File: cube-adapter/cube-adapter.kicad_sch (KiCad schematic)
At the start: 40 parts, among them J1 Conn_01x02, J10 Conn_01x02, J11 Conn_01x03, J12 Conn_01x03, J13 Conn_01x03, J14 Conn_01x03, J15 Conn_01x03, J16 Conn_01x03, J17 Conn_01x03, J18 Conn_01x03, J19 Conn_01x03, J2 Conn_01x02, J20 Conn_01x03, J21 Conn_01x03, J22 Conn_01x03, J23 Conn_01x06, J24 Conn_01x06, J25 Conn_01x04, J26 Conn_01x04, J27 Conn_01x05, J28 Conn_01x05, J29 Conn_01x05, J3 Conn_01x02, J30 Conn_01x04, J31 Conn_01x04, J32 Conn_01x04, J33 Conn_01x03, J34 Conn_01x03, J35 Conn_01x03, J36 Conn_01x02, J37 Conn_01x02, J38 Conn_01x02, J4 Conn_01x02, J5 Conn_01x02, J6 Conn_01x02, J7 Conn_01x02, J8 Conn_01x02, J9 Conn_01x02, U1 MEGA_PRO_EMBED_CH340G___ATMEG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

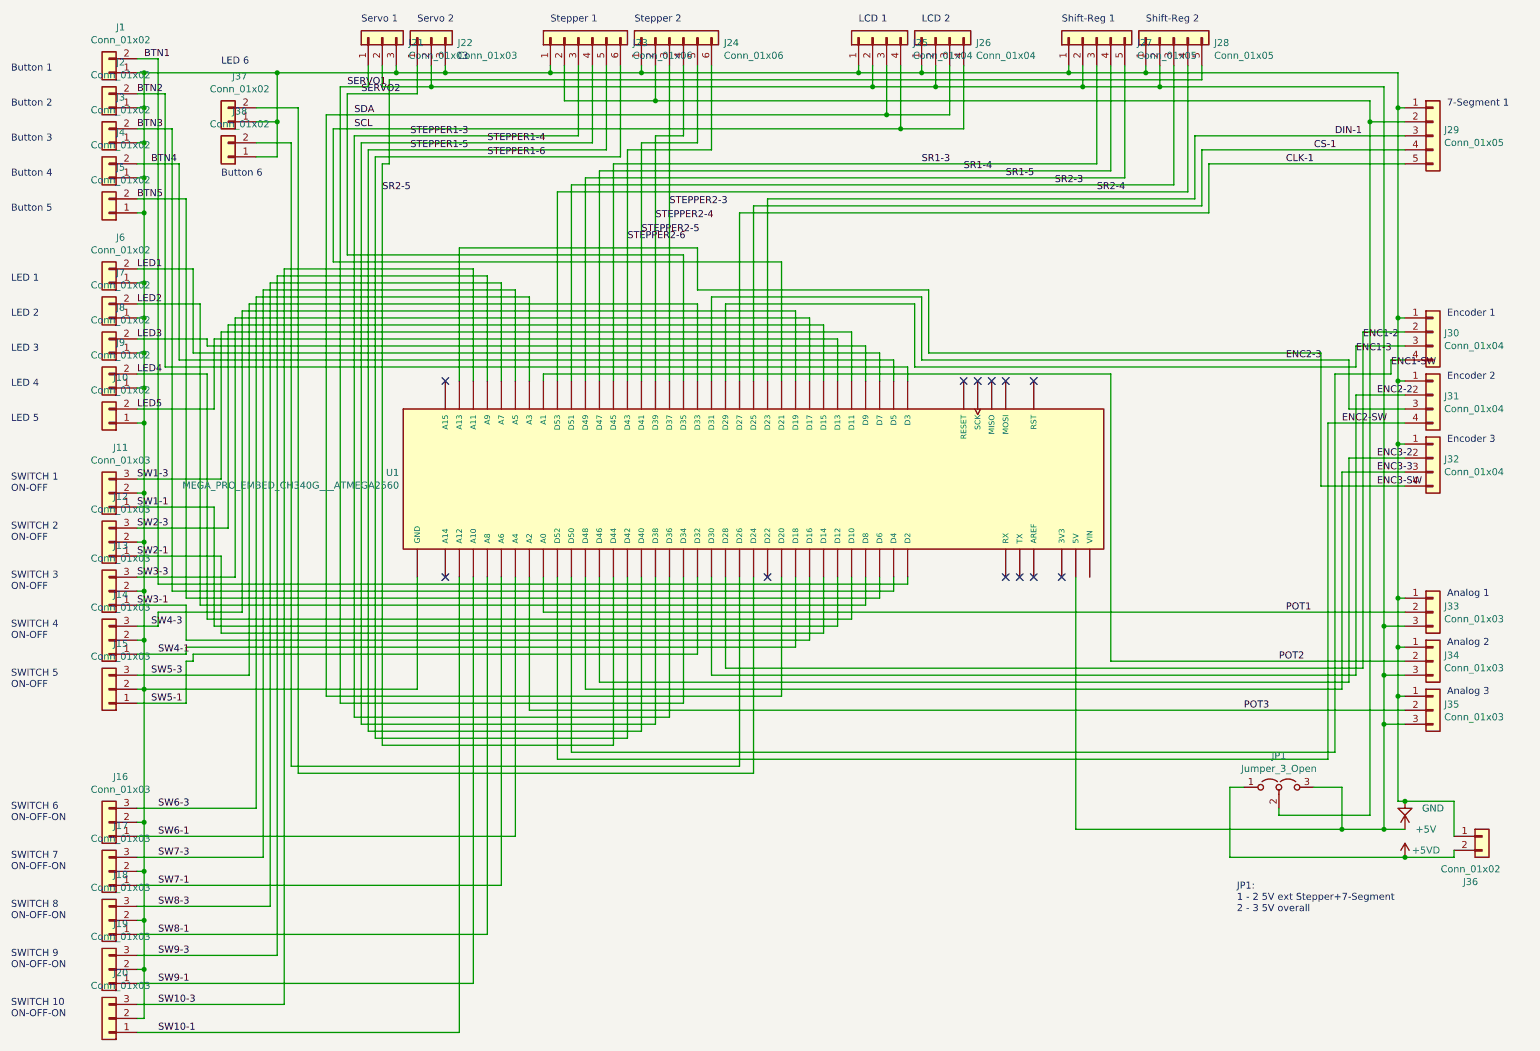
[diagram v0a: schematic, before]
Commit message: Added the cube adapter changes
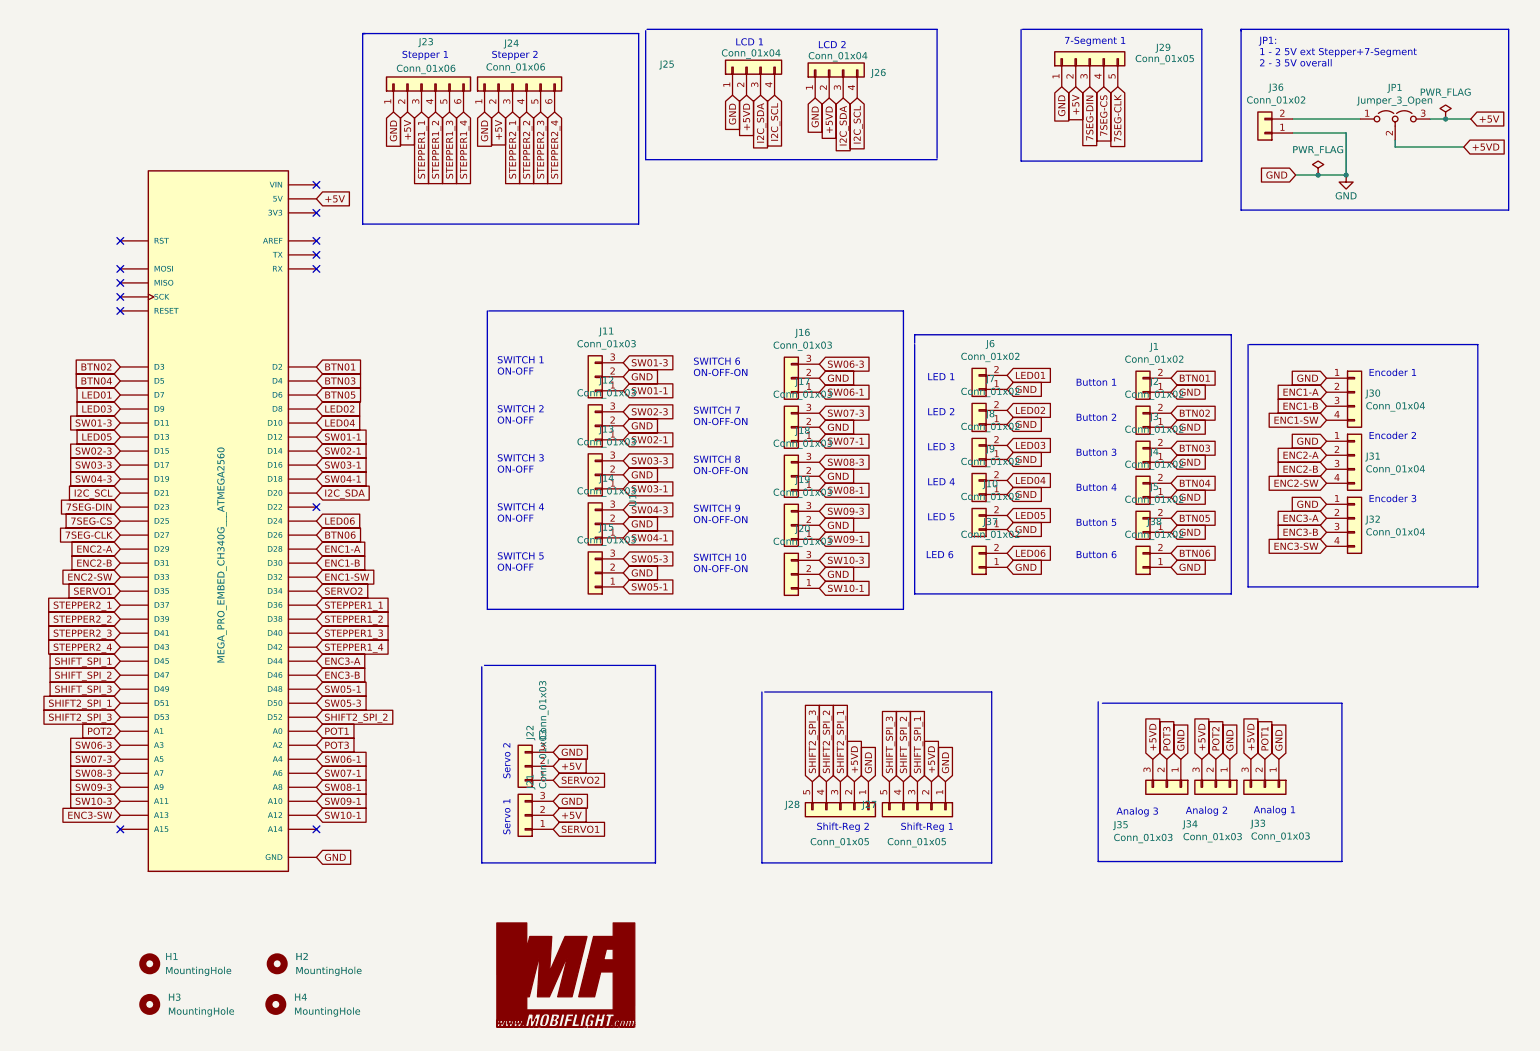
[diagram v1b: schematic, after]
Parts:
- added H1, H2, H3, H4: MountingHole, MountingHole:MountingHole_3.5mm, symbol Mechanical:MountingHole
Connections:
- net +5V: now also J23.2 (Pin_2), J24.2 (Pin_2), J29.2 (Pin_2); no longer J25.2 (Pin_2), J26.2 (Pin_2), J27.2 (Pin_2), J28.2 (Pin_2), J33.3 (Pin_3), J34.3 (Pin_3), J35.3 (Pin_3)
- net +5VD: now also J25.2 (Pin_2), J26.2 (Pin_2), J27.2 (Pin_2), J28.2 (Pin_2), J33.3 (Pin_3), J34.3 (Pin_3), J35.3 (Pin_3), JP1.2 (C); no longer J36.2 (Pin_2), JP1.1 (A)
- net ENC1-SW: now also U1.D32; no longer U1.D50
- net ENC2-SW: now also U1.D33; no longer U1.D52
- net SERVO1: now also U1.D35; no longer U1.D34
- net SERVO2: now also U1.D34; no longer U1.D35
- net LED06: now reaches J37.2 (Pin_2), U1.D24
- net BTN06: now reaches J38.2 (Pin_2), U1.D26
- net BTN1 renamed BTN01
- net BTN2 renamed BTN02
- net BTN3 renamed BTN03
- net BTN4 renamed BTN04
- net BTN5 renamed BTN05
- net CLK-1 renamed 7SEG-CLK
- net CS-1 renamed 7SEG-CS
- net DIN-1 renamed 7SEG-DIN
- net ENC1-2 renamed ENC1-A
- net ENC1-3 renamed ENC1-B
- net ENC1-B: now also U1.D30; no longer U1.D29
- net ENC2-2 renamed ENC2-A
- net ENC2-A: now also U1.D29; no longer U1.D30
- net ENC2-3 renamed ENC2-B
- net ENC3-2 renamed ENC3-A
- net ENC3-A: now also U1.D44; no longer U1.D46
- net ENC3-3 renamed ENC3-B
- net ENC3-B: now also U1.D46; no longer U1.D48
- net LED1 renamed LED01
- net LED2 renamed LED02
- net LED3 renamed LED03
- net LED4 renamed LED04
- net LED5 renamed LED05
- net SCL renamed I2C_SCL
- net SDA renamed I2C_SDA
- net SR1-3 renamed SHIFT_SPI_1
- net SR1-4 renamed SHIFT_SPI_2
- net SR1-5 renamed SHIFT_SPI_3
- net SR2-3 renamed SHIFT2_SPI_1
- net SR2-4 renamed SHIFT2_SPI_2
- net SHIFT2_SPI_2: now also U1.D52; no longer U1.D53
- net SR2-5 renamed SHIFT2_SPI_3
- net SHIFT2_SPI_3: now also U1.D53; no longer U1.D44
- net STEPPER1-3 renamed STEPPER1_1
- net STEPPER1-4 renamed STEPPER1_2
- net STEPPER1-5 renamed STEPPER1_3
- net STEPPER1-6 renamed STEPPER1_4
- net STEPPER2-3 renamed STEPPER2_1
- net STEPPER2-4 renamed STEPPER2_2
- net STEPPER2-5 renamed STEPPER2_3
- net STEPPER2-6 renamed STEPPER2_4
- net SW1-1 renamed SW01-1
- net SW1-3 renamed SW01-3
- net SW2-1 renamed SW02-1
- net SW2-3 renamed SW02-3
- net SW3-1 renamed SW03-1
- net SW3-3 renamed SW03-3
- net SW4-1 renamed SW04-1
- net SW4-3 renamed SW04-3
- net SW5-1 renamed SW05-1
- net SW05-1: now also U1.D48; no longer U1.D32
- net SW5-3 renamed SW05-3
- net SW05-3: now also U1.D50; no longer U1.D33
- net SW6-1 renamed SW06-1
- net SW6-3 renamed SW06-3
- net SW7-1 renamed SW07-1
- net SW7-3 renamed SW07-3
- net SW8-1 renamed SW08-1
- net SW8-3 renamed SW08-3
- net SW9-1 renamed SW09-1
- net SW9-3 renamed SW09-3
- new net: J36.2 (Pin_2), JP1.1 (A)
- no-connect marks 12 -> 13
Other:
- company: (none) -> mobiflight community
- moved on the sheet: J1, J10, J11, J12, J13, J14, J15, J16, J17, J18, J19, J2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

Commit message: v2.0 of cube adapter
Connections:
- net +5V: no longer J21.2 (Pin_2), J22.2 (Pin_2), J23.2 (Pin_2), J24.2 (Pin_2), J29.2 (Pin_2)
- net +5VD: now also J21.2 (Pin_2), J22.2 (Pin_2), J23.2 (Pin_2), J24.2 (Pin_2), J29.2 (Pin_2)
- net GND: now also J11.1 (Pin_1), J12.1 (Pin_1), J13.1 (Pin_1), J14.1 (Pin_1), J15.1 (Pin_1), J16.1 (Pin_1), J17.1 (Pin_1), J18.1 (Pin_1), J19.1 (Pin_1), J20.1 (Pin_1), J21.1 (Pin_1), J22.1 (Pin_1); no longer J11.2 (Pin_2), J12.2 (Pin_2), J13.2 (Pin_2), J14.2 (Pin_2), J15.2 (Pin_2), J16.2 (Pin_2), J17.2 (Pin_2), J18.2 (Pin_2), J19.2 (Pin_2), J20.2 (Pin_2), J21.3 (Pin_3), J22.3 (Pin_3)
- net SERVO1: now also J21.3 (Pin_3); no longer J21.1 (Pin_1)
- net SERVO2: now also J22.3 (Pin_3); no longer J22.1 (Pin_1)
- net SW01-1: now also J11.2 (Pin_2); no longer J11.1 (Pin_1)
- net SW02-1: now also J12.2 (Pin_2); no longer J12.1 (Pin_1)
- net SW03-1: now also J13.2 (Pin_2); no longer J13.1 (Pin_1)
- net SW04-1: now also J14.2 (Pin_2); no longer J14.1 (Pin_1)
- net SW05-1: now also J15.2 (Pin_2); no longer J15.1 (Pin_1)
- net SW06-1: now also J16.2 (Pin_2); no longer J16.1 (Pin_1)
- net SW07-1: now also J17.2 (Pin_2); no longer J17.1 (Pin_1)
- net SW08-1: now also J18.2 (Pin_2); no longer J18.1 (Pin_1)
- net SW09-1: now also J19.2 (Pin_2); no longer J19.1 (Pin_1)
- net SW10-1: now also J20.2 (Pin_2); no longer J20.1 (Pin_1)

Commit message: Prototyping board - Updated pictures and schematic
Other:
- title: Cube-System MobiFlight -> MobiFlight Prototyping Board
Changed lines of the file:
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@@
   (paper "A4")
   (title_block
-    (title "Cube-System MobiFlight")
+    (title "MobiFlight Prototyping Board")
     (date "09.12.2022")
-    (rev "1.4")
+    (rev "2.0")
     (company "mobiflight community")
     (comment 1 "stephan hoeltig")

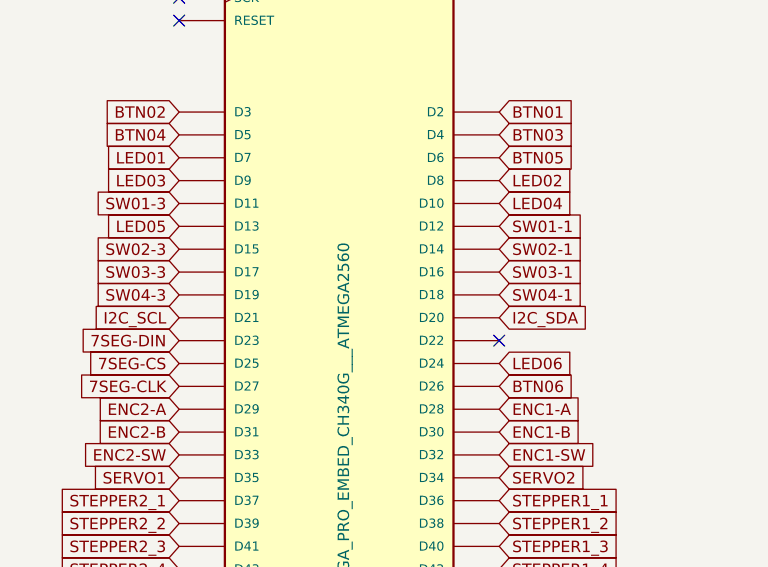
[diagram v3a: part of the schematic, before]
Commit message: switch led pin and fix labels
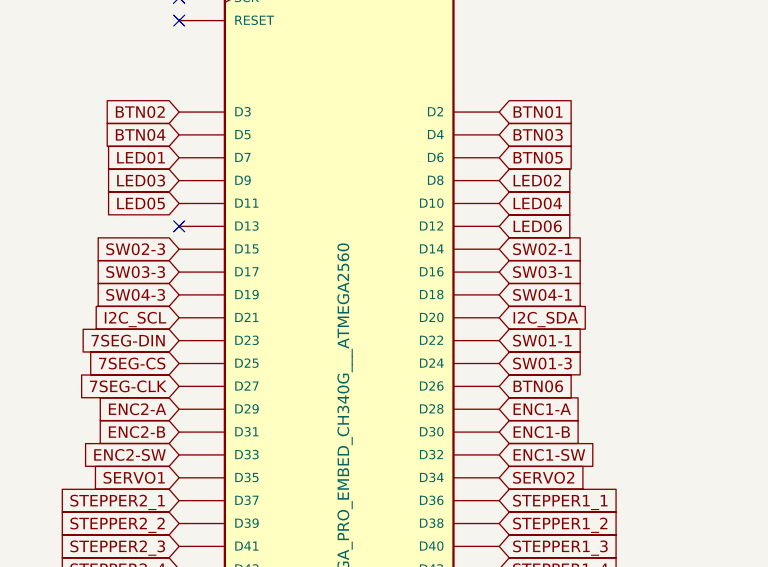
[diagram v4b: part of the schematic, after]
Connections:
- net LED05: now also U1.D11; no longer U1.D13
- net LED06: now also U1.D12; no longer U1.D24
- net SW01-1: now also U1.D22; no longer U1.D12
- net SW01-3: now also U1.D24; no longer U1.D11
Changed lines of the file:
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@@
     (title "MobiFlight Prototyping Board")
     (date "09.12.2022")
-    (rev "2.0")
+    (rev "2.1")
     (company "mobiflight community")
     (comment 1 "stephan hoeltig")
@@
   (no_connect (at 32.512 157.48))
   (no_connect (at 68.072 50.8))
-  (no_connect (at 68.072 99.06))
+  (no_connect (at 32.512 86.36))
   (no_connect (at 68.072 157.48))
   (no_connect (at 32.512 63.5))
@@
     )
   )
-  (global_label "SW01-3" (shape input) (at 32.512 83.82 180) (fields_autoplaced)
-    (effects (font (size 1.27 1.27)) (justify right))
-    (property "Intersheet References" "${INTERSHEET_REFS}" (id 0) (at 22.3259 83.8994 0)
-      (effects (font (size 1.27 1.27)) (justify right) hide)
+  (global_label "SW01-3" (shape input) (at 68.072 101.6 0) (fields_autoplaced)
+    (effects (font (size 1.27 1.27)) (justify left))
+    (property "Intersheet References" "${INTERSHEET_REFS}" (id 0) (at 78.2581 101.6794 0)
+      (effects (font (size 1.27 1.27)) (justify left) hide)
     )
   )
@@
     )
   )
-  (global_label "LED06" (shape input) (at 68.072 101.6 0) (fields_autoplaced)
-    (effects (font (size 1.27 1.27)) (justify left))
-    (property "Intersheet References" "${INTERSHEET_REFS}" (id 0) (at 76.2624 101.5206 0)
+  (global_label "LED06" (shape input) (at 68.072 86.36 0) (fields_autoplaced)
+    (effects (font (size 1.27 1.27)) (justify left))
+    (property "Intersheet References" "${INTERSHEET_REFS}" (id 0) (at 76.2624 86.2806 0)
       (effects (font (size 1.27 1.27)) (justify left) hide)
     )
@@
     )
   )
-  (global_label "SW01-1" (shape input) (at 68.072 86.36 0) (fields_autoplaced)
-    (effects (font (size 1.27 1.27)) (justify left))
-    (property "Intersheet References" "${INTERSHEET_REFS}" (id 0) (at 78.2581 86.2806 0)
+  (global_label "SW01-1" (shape input) (at 68.072 99.06 0) (fields_autoplaced)
+    (effects (font (size 1.27 1.27)) (justify left))
+    (property "Intersheet References" "${INTERSHEET_REFS}" (id 0) (at 78.2581 98.9806 0)
       (effects (font (size 1.27 1.27)) (justify left) hide)
     )
@@
     )
   )
-  (global_label "LED05" (shape input) (at 32.512 86.36 180) (fields_autoplaced)
-    (effects (font (size 1.27 1.27)) (justify right))
-    (property "Intersheet References" "${INTERSHEET_REFS}" (id 0) (at 24.3216 86.4394 0)
-      (effects (font (size 1.27 1.27)) (justify right) hide)
-    )
+  (global_label "LED05" (shape input) (at 32.512 83.82 180) (fields_autoplaced)
+    (effects (font (size 1.27 1.27)) (justify right))
+    (property "Intersheet References" "${INTERSHEET_REFS}" (id 0) (at 24.3216 83.8994 0)
+      (effects (font (size 1.27 1.27)) (justify right) hide)
+    )
